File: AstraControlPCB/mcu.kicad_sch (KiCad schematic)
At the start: 9 parts, among them U1 ESP32-S3-WROOM-1U-N8

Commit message: Update wks file
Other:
- company: (none) -> LiveAstra Technologies
- title: MCU -> AstraControl - Root
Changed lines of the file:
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@@
 	(paper "A4")
 	(title_block
-		(title "MCU")
+		(title "AstraControl - Root")
+		(date "2024-08-26")
+		(rev "A")
+		(company "LiveAstra Technologies")
 	)
 	(junction

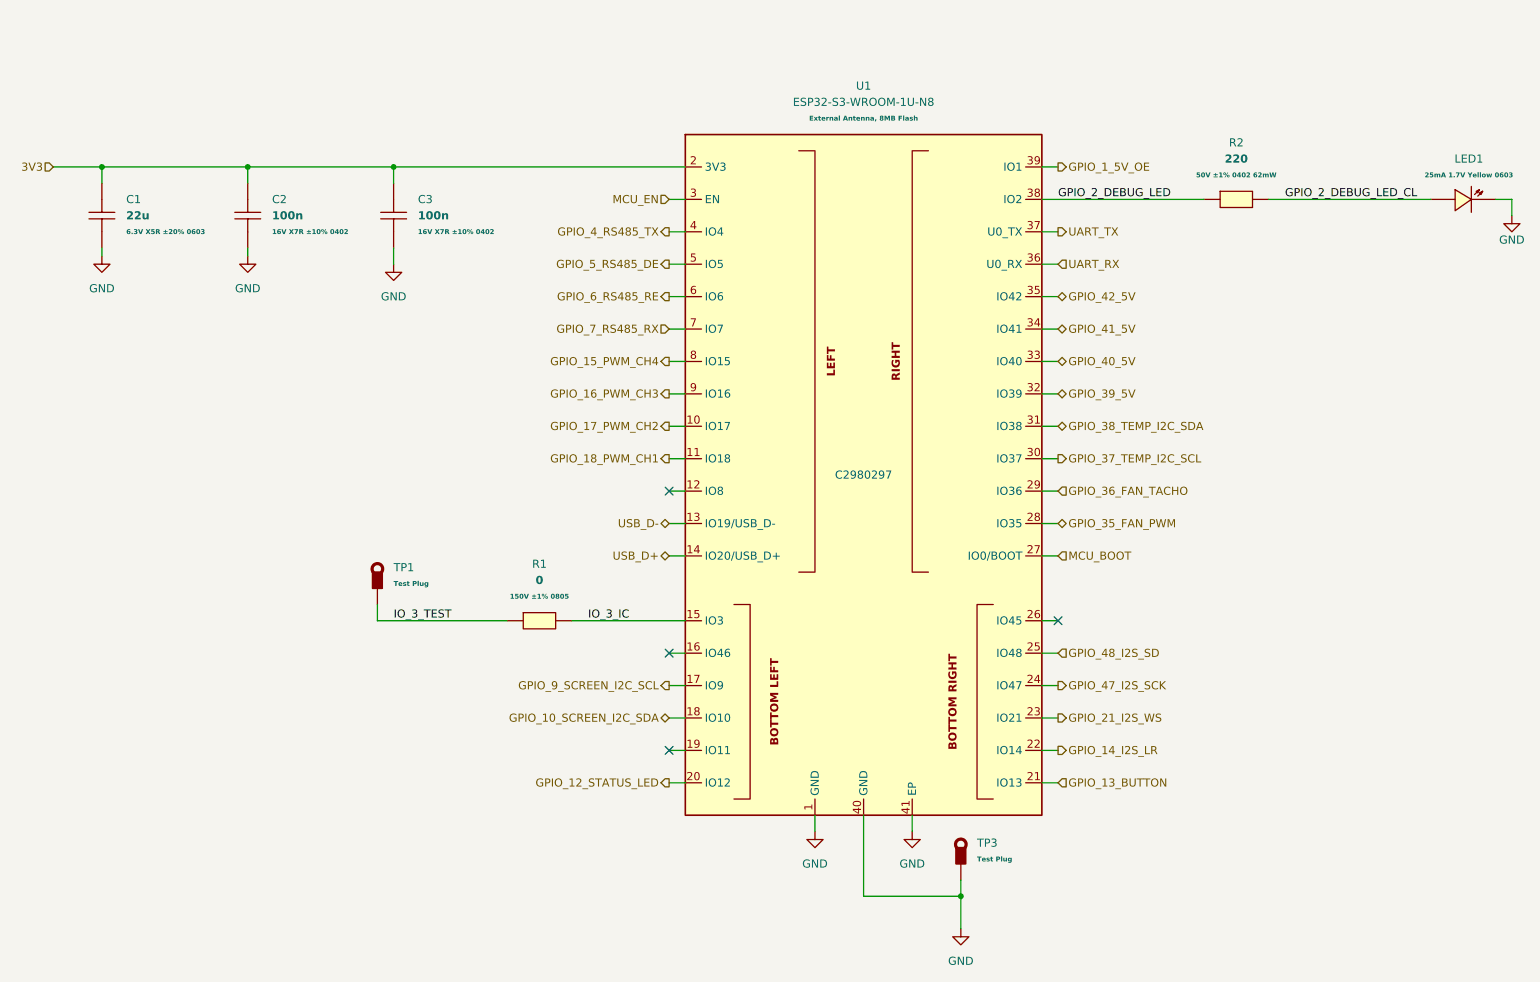
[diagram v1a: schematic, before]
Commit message: Remove plus minus symbol
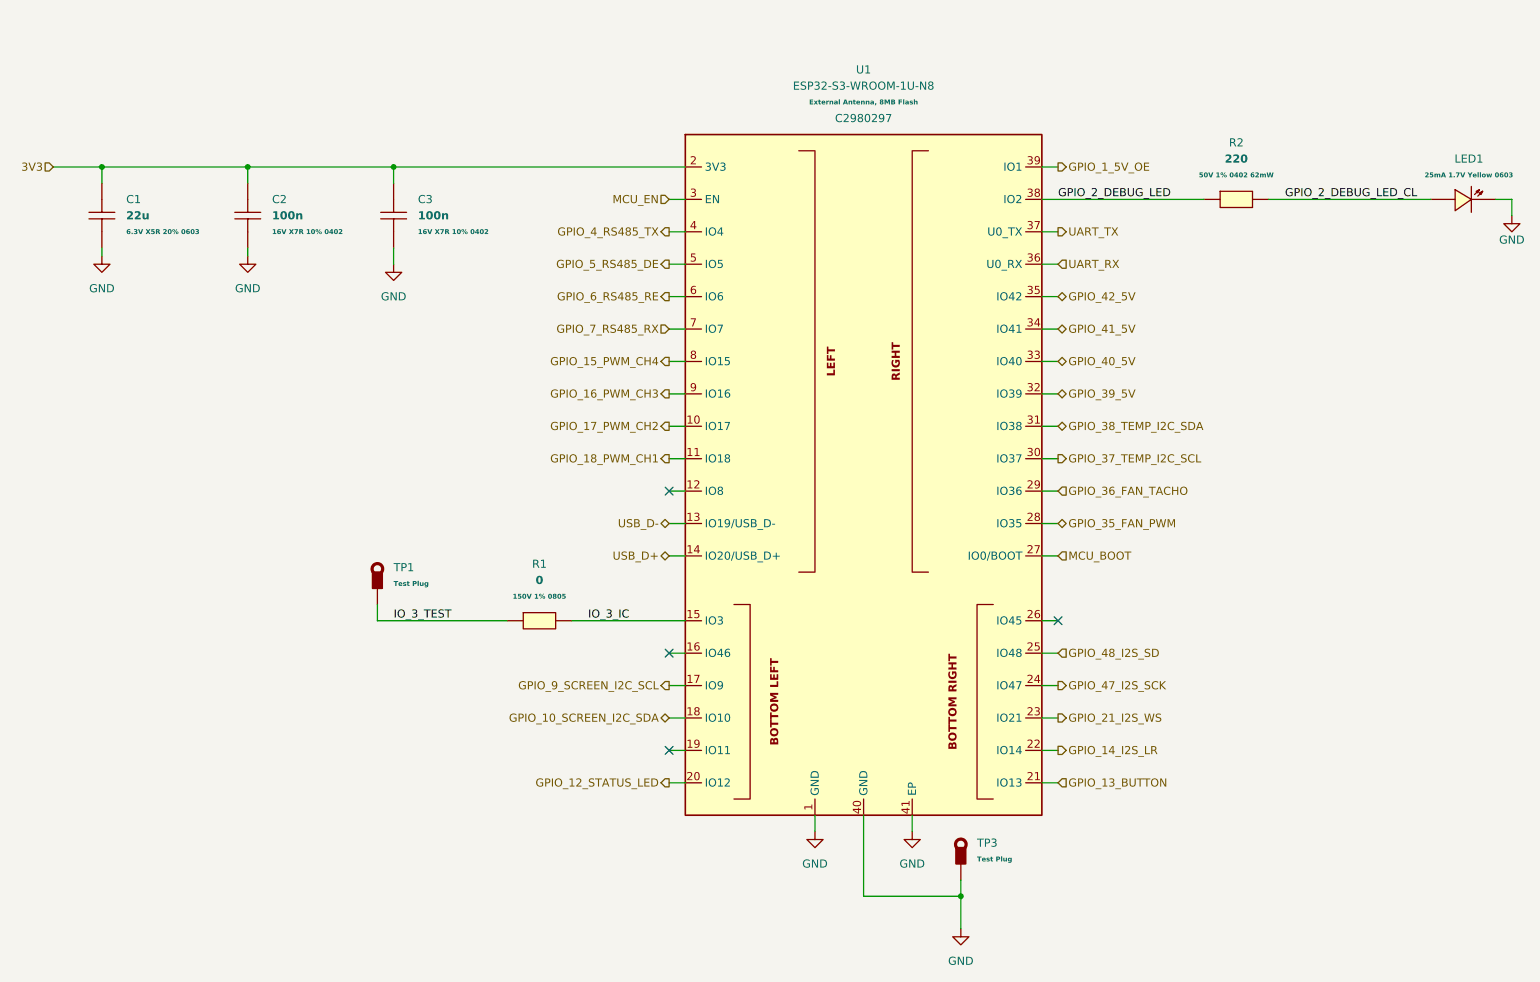
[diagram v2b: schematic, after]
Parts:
- C1: Extra Values 6.3V X5R ±20% 0603 -> 6.3V X5R 20% 0603
- C2, C3: Extra Values 16V X7R ±10% 0402 -> 16V X7R 10% 0402
- R1: Extra Values 150V ±1% 0805 -> 150V 1% 0805
- R2: Extra Values 50V ±1% 0402 62mW -> 50V 1% 0402 62mW
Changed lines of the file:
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@@
 			)
 		)
-		(property "Extra Values" "16V X7R ±10% 0402"
+		(property "Extra Values" "16V X7R 10% 0402"
 			(at 59.69 55.8799 90)
 			(effects
@@
 				)
 				(justify right)
-			)
-		)
-		(property "Extra Value" ""
-			(at 55.88 53.34 0)
-			(effects
-				(font
-					(size 1.27 1.27)
-				)
-				(hide yes)
 			)
 		)
@@
 		(dnp no)
 		(fields_autoplaced yes)
-		(property "Reference" "#PWR05"
+		(property "Reference" "#PWR5"
 			(at 55.88 66.04 0)
 			(effects
@@
 			(project "AstraControl"
 				(path "/9a751838-dce8-4d69-8a02-736625ac74e7/0db21d8e-3390-4d67-877f-0e5d98e37848/3087dd4a-2a8a-4df4-b1d8-8d4a2b3256a2"
-					(reference "#PWR05")
+					(reference "#PWR5")
 					(unit 1)
 				)
@@
 			)
 		)
-		(property "Extra Value" ""
-			(at 246.38 50.8 0)
-			(effects
-				(font
-					(size 1.27 1.27)
-				)
-				(hide yes)
-			)
-		)
 		(pin "1"
 		)
@@
 			)
 		)
-		(property "Extra Values" "6.3V X5R ±20% 0603"
+		(property "Extra Values" "6.3V X5R 20% 0603"
 			(at 36.83 55.8799 90)
 			(effects
@@
 				)
 				(justify right)
-			)
-		)
-		(property "Extra Value" ""
-			(at 33.02 53.34 0)
-			(effects
-				(font
-					(size 1.27 1.27)
-				)
-				(hide yes)
 			)
 		)
@@
 			)
 		)
-		(property "Extra Values" "50V ±1% 0402 62mW"
+		(property "Extra Values" "50V 1% 0402 62mW"
 			(at 210.82 46.99 0)
 			(effects
@@
 					(bold yes)
 				)
-			)
-		)
-		(property "Extra Value" ""
-			(at 210.82 50.8 0)
-			(effects
-				(font
-					(size 1.27 1.27)
-				)
-				(hide yes)
 			)
 		)
@@
 			)
 		)
-		(property "Extra Value" ""
-			(at 167.64 157.48 0)
-			(effects
-				(font
-					(size 1.27 1.27)
-				)
-				(hide yes)
-			)
-		)
 		(pin "1"
 		)
@@
 		(dnp no)
 		(fields_autoplaced yes)
-		(property "Reference" "#PWR04"
+		(property "Reference" "#PWR4"
 			(at 33.02 66.04 0)
 			(effects
@@
 			(project "AstraControl"
 				(path "/9a751838-dce8-4d69-8a02-736625ac74e7/0db21d8e-3390-4d67-877f-0e5d98e37848/3087dd4a-2a8a-4df4-b1d8-8d4a2b3256a2"
-					(reference "#PWR04")
+					(reference "#PWR4")
 					(unit 1)
 				)
@@
 			)
 		)
-		(property "Extra Values" "16V X7R ±10% 0402"
+		(property "Extra Values" "16V X7R 10% 0402"
 			(at 82.55 55.8799 90)
 			(effects
@@
 				)
 				(justify right)
-			)
-		)
-		(property "Extra Value" ""
-			(at 78.74 53.34 0)
-			(effects
-				(font
-					(size 1.27 1.27)
-				)
-				(hide yes)
 			)
 		)
@@
 		(dnp no)
 		(fields_autoplaced yes)
-		(property "Reference" "#PWR06"
+		(property "Reference" "#PWR6"
 			(at 78.74 67.31 0)
 			(effects
@@
 			(project "AstraControl"
 				(path "/9a751838-dce8-4d69-8a02-736625ac74e7/0db21d8e-3390-4d67-877f-0e5d98e37848/3087dd4a-2a8a-4df4-b1d8-8d4a2b3256a2"
-					(reference "#PWR06")
+					(reference "#PWR6")
 					(unit 1)
 				)
@@
 		(dnp no)
 		(fields_autoplaced yes)
-		(property "Reference" "#PWR08"
+		(property "Reference" "#PWR8"
 			(at 160.02 156.21 0)
 			(effects
@@
 			(project "AstraControl"
 				(path "/9a751838-dce8-4d69-8a02-736625ac74e7/0db21d8e-3390-4d67-877f-0e5d98e37848/3087dd4a-2a8a-4df4-b1d8-8d4a2b3256a2"
-					(reference "#PWR08")
+					(reference "#PWR8")
 					(unit 1)
 				)
@@
 		(on_board yes)
 		(dnp no)
-		(property "Reference" "#PWR010"
+		(property "Reference" "#PWR10"
 			(at 254 59.69 0)
 			(effects
@@
 			(project "AstraControl"
 				(path "/9a751838-dce8-4d69-8a02-736625ac74e7/0db21d8e-3390-4d67-877f-0e5d98e37848/3087dd4a-2a8a-4df4-b1d8-8d4a2b3256a2"
-					(reference "#PWR010")
+					(reference "#PWR10")
 					(unit 1)
 				)
@@
 		(dnp no)
 		(fields_autoplaced yes)
-		(property "Reference" "#PWR09"
+		(property "Reference" "#PWR9"
 			(at 167.64 171.45 0)
 			(effects
@@
 			(project "AstraControl"
 				(path "/9a751838-dce8-4d69-8a02-736625ac74e7/0db21d8e-3390-4d67-877f-0e5d98e37848/3087dd4a-2a8a-4df4-b1d8-8d4a2b3256a2"
-					(reference "#PWR09")
+					(reference "#PWR9")
 					(unit 1)
 				)
@@
 		(dnp no)
 		(fields_autoplaced yes)
-		(property "Reference" "#PWR07"
+		(property "Reference" "#PWR7"
 			(at 144.78 156.21 0)
 			(effects
@@
 			(project "AstraControl"
 				(path "/9a751838-dce8-4d69-8a02-736625ac74e7/0db21d8e-3390-4d67-877f-0e5d98e37848/3087dd4a-2a8a-4df4-b1d8-8d4a2b3256a2"
-					(reference "#PWR07")
+					(reference "#PWR7")
 					(unit 1)
 				)
@@
 			)
 		)
-		(property "Extra Values" "150V ±1% 0805"
+		(property "Extra Values" "150V 1% 0805"
 			(at 101.6 113.03 0)
 			(effects
@@
 					(bold yes)
 				)
-			)
-		)
-		(property "Extra Value" ""
-			(at 101.6 116.84 0)
-			(effects
-				(font
-					(size 1.27 1.27)
-				)
-				(hide yes)
 			)
 		)
@@
 		(fields_autoplaced yes)
 		(property "Reference" "U1"
+			(at 152.4 30.48 0)
+			(effects
+				(font
+					(size 1.27 1.27)
+				)
+			)
+		)
+		(property "Value" "ESP32-S3-WROOM-1U-N8"
 			(at 152.4 33.02 0)
-			(effects
-				(font
-					(size 1.27 1.27)
-				)
-			)
-		)
-		(property "Value" "ESP32-S3-WROOM-1U-N8"
-			(at 152.4 35.56 0)
 			(effects
 				(font
@@
 		)
 		(property "Extra Values" "External Antenna, 8MB Flash"
+			(at 152.4 35.56 0)
+			(effects
+				(font
+					(size 0.762 0.762)
+					(bold yes)
+				)
+			)
+		)
+		(property "LCSC Part" "C2980297"
 			(at 152.4 38.1 0)
 			(effects
 				(font
-					(size 0.762 0.762)
-					(bold yes)
-				)
-			)
-		)
-		(property "LCSC Part" "C2980297"
-			(at 152.4 93.98 0)
-			(effects
-				(font
-					(size 1.27 1.27)
-				)
-			)
-		)
-		(property "Extra Value" ""
-			(at 152.4 93.98 0)
-			(effects
-				(font
-					(size 1.27 1.27)
-				)
-				(hide yes)
+					(size 1.27 1.27)
+				)
 			)
 		)
@@
 			)
 		)
-		(property "Extra Value" ""
-			(at 76.2 114.3 0)
-			(effects
-				(font
-					(size 1.27 1.27)
-				)
-				(hide yes)
-			)
-		)

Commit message: workflow
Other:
- note added: "MCU"
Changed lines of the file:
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@@
+		)
+	)
+	(text "MCU"
+		(exclude_from_sim no)
+		(at 19.05 25.4 0)
+		(effects
+			(font
+				(face "ING Me Headline")
+				(size 8 8)
+			)
+			(justify left top)
 		)
 	)
@@
 		(dnp no)
 		(fields_autoplaced yes)
-		(property "Reference" "#PWR5"
+		(property "Reference" "#PWR05"
 			(at 55.88 66.04 0)
 			(effects
@@
 			(project "AstraControl"
 				(path "/9a751838-dce8-4d69-8a02-736625ac74e7/0db21d8e-3390-4d67-877f-0e5d98e37848/3087dd4a-2a8a-4df4-b1d8-8d4a2b3256a2"
-					(reference "#PWR5")
+					(reference "#PWR05")
 					(unit 1)
 				)
@@
 		(dnp no)
 		(fields_autoplaced yes)
-		(property "Reference" "#PWR4"
+		(property "Reference" "#PWR04"
 			(at 33.02 66.04 0)
 			(effects
@@
 			(project "AstraControl"
 				(path "/9a751838-dce8-4d69-8a02-736625ac74e7/0db21d8e-3390-4d67-877f-0e5d98e37848/3087dd4a-2a8a-4df4-b1d8-8d4a2b3256a2"
-					(reference "#PWR4")
+					(reference "#PWR04")
 					(unit 1)
 				)
@@
 		(dnp no)
 		(fields_autoplaced yes)
-		(property "Reference" "#PWR6"
+		(property "Reference" "#PWR06"
 			(at 78.74 67.31 0)
 			(effects
@@
 			(project "AstraControl"
 				(path "/9a751838-dce8-4d69-8a02-736625ac74e7/0db21d8e-3390-4d67-877f-0e5d98e37848/3087dd4a-2a8a-4df4-b1d8-8d4a2b3256a2"
-					(reference "#PWR6")
+					(reference "#PWR06")
 					(unit 1)
 				)
@@
 		(dnp no)
 		(fields_autoplaced yes)
-		(property "Reference" "#PWR8"
+		(property "Reference" "#PWR08"
 			(at 160.02 156.21 0)
 			(effects
@@
 			(project "AstraControl"
 				(path "/9a751838-dce8-4d69-8a02-736625ac74e7/0db21d8e-3390-4d67-877f-0e5d98e37848/3087dd4a-2a8a-4df4-b1d8-8d4a2b3256a2"
-					(reference "#PWR8")
+					(reference "#PWR08")
 					(unit 1)
 				)
@@
 		(on_board yes)
 		(dnp no)
-		(property "Reference" "#PWR10"
+		(property "Reference" "#PWR010"
 			(at 254 59.69 0)
 			(effects
@@
 			(project "AstraControl"
 				(path "/9a751838-dce8-4d69-8a02-736625ac74e7/0db21d8e-3390-4d67-877f-0e5d98e37848/3087dd4a-2a8a-4df4-b1d8-8d4a2b3256a2"
-					(reference "#PWR10")
+					(reference "#PWR010")
 					(unit 1)
 				)
@@
 		(dnp no)
 		(fields_autoplaced yes)
-		(property "Reference" "#PWR9"
+		(property "Reference" "#PWR09"
 			(at 167.64 171.45 0)
 			(effects
@@
 			(project "AstraControl"
 				(path "/9a751838-dce8-4d69-8a02-736625ac74e7/0db21d8e-3390-4d67-877f-0e5d98e37848/3087dd4a-2a8a-4df4-b1d8-8d4a2b3256a2"
-					(reference "#PWR9")
+					(reference "#PWR09")
 					(unit 1)
 				)
@@
 		(dnp no)
 		(fields_autoplaced yes)
-		(property "Reference" "#PWR7"
+		(property "Reference" "#PWR07"
 			(at 144.78 156.21 0)
 			(effects
@@
 			(project "AstraControl"
 				(path "/9a751838-dce8-4d69-8a02-736625ac74e7/0db21d8e-3390-4d67-877f-0e5d98e37848/3087dd4a-2a8a-4df4-b1d8-8d4a2b3256a2"
-					(reference "#PWR7")
+					(reference "#PWR07")
 					(unit 1)
 				)

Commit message: update
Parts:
- renumbered TP3 to TP2
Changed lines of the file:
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@@
 		(dnp no)
 		(fields_autoplaced yes)
-		(property "Reference" "TP3"
+		(property "Reference" "TP2"
 			(at 170.18 151.6676 0)
 			(effects
@@
 			(project "AstraControl"
 				(path "/9a751838-dce8-4d69-8a02-736625ac74e7/0db21d8e-3390-4d67-877f-0e5d98e37848/3087dd4a-2a8a-4df4-b1d8-8d4a2b3256a2"
-					(reference "TP3")
+					(reference "TP2")
 					(unit 1)
 				)

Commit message: Reroute complete
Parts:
- removed C1: 22u, LiveAstra:C_0603_1608Metric, symbol LiveAstra:C_22uF_X5R_0603
- added C19: 47u, LiveAstra:C_0805_2012Metric_Pad1.18x1.45mm_HandSolder, symbol LiveAstra:C_47u_X5R_0805
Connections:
- net 3V3: now also C19.2
- net GND: now also C19.1
- net GPIO_35_FAN_PWM renamed GPIO_35_TEMP_I2C_SCL
- net GPIO_36_FAN_TACHO renamed GPIO_36_TEMP_I2C_SDA
- net GPIO_37_TEMP_I2C_SCL renamed GPIO_37_FAN_PWM
- net GPIO_38_TEMP_I2C_SDA renamed GPIO_38_FAN_TACHO
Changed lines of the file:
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@@
+	(wire
+		(pts
+			(xy 180.34 91.44) (xy 182.88 91.44)
+		)
+		(stroke
+			(width 0)
+			(type default)
+		)
+	)
 	(wire
 		(pts
@@
 	(wire
 		(pts
-			(xy 182.88 91.44) (xy 180.34 91.44)
-		)
-		(stroke
-			(width 0)
-			(type default)
-		)
-	)
-	(wire
-		(pts
 			(xy 33.02 48.26) (xy 33.02 45.72)
 		)
@@
 	(wire
 		(pts
-			(xy 182.88 86.36) (xy 180.34 86.36)
-		)
-		(stroke
-			(width 0)
-			(type default)
-		)
-	)
-	(wire
-		(pts
 			(xy 55.88 48.26) (xy 55.88 45.72)
 		)
@@
 	(wire
 		(pts
+			(xy 180.34 101.6) (xy 182.88 101.6)
+		)
+		(stroke
+			(width 0)
+			(type default)
+		)
+	)
+	(wire
+		(pts
 			(xy 182.88 142.24) (xy 180.34 142.24)
 		)
@@
 	(wire
 		(pts
+			(xy 180.34 86.36) (xy 182.88 86.36)
+		)
+		(stroke
+			(width 0)
+			(type default)
+		)
+	)
+	(wire
+		(pts
 			(xy 121.92 71.12) (xy 124.46 71.12)
 		)
@@
 	(wire
 		(pts
+			(xy 180.34 96.52) (xy 182.88 96.52)
+		)
+		(stroke
+			(width 0)
+			(type default)
+		)
+	)
+	(wire
+		(pts
 			(xy 180.34 71.12) (xy 182.88 71.12)
 		)
@@
 		(pts
 			(xy 180.34 60.96) (xy 182.88 60.96)
-		)
-		(stroke
-			(width 0)
-			(type default)
-		)
-	)
-	(wire
-		(pts
-			(xy 182.88 101.6) (xy 180.34 101.6)
-		)
-		(stroke
-			(width 0)
-			(type default)
-		)
-	)
-	(wire
-		(pts
-			(xy 182.88 96.52) (xy 180.34 96.52)
 		)
 		(stroke
@@
 		)
 	)
-	(hierarchical_label "GPIO_38_TEMP_I2C_SDA"
+	(hierarchical_label "GPIO_36_TEMP_I2C_SDA"
 		(shape bidirectional)
-		(at 182.88 86.36 0)
+		(at 182.88 96.52 0)
 		(fields_autoplaced yes)
 		(effects
@@
 		)
 	)
-	(hierarchical_label "GPIO_37_TEMP_I2C_SCL"
+	(hierarchical_label "GPIO_35_TEMP_I2C_SCL"
 		(shape output)
-		(at 182.88 91.44 0)
+		(at 182.88 101.6 0)
 		(fields_autoplaced yes)
 		(effects
@@
 		)
 	)
-	(hierarchical_label "GPIO_35_FAN_PWM"
+	(hierarchical_label "GPIO_37_FAN_PWM"
 		(shape bidirectional)
-		(at 182.88 101.6 0)
+		(at 182.88 91.44 0)
 		(fields_autoplaced yes)
 		(effects
@@
 		)
 	)
-	(hierarchical_label "GPIO_36_FAN_TACHO"
+	(hierarchical_label "GPIO_38_FAN_TACHO"
 		(shape input)
-		(at 182.88 96.52 0)
+		(at 182.88 86.36 0)
 		(fields_autoplaced yes)
 		(effects
@@
 				(path "/9a751838-dce8-4d69-8a02-736625ac74e7/0db21d8e-3390-4d67-877f-0e5d98e37848/3087dd4a-2a8a-4df4-b1d8-8d4a2b3256a2"
 					(reference "LED1")
-					(unit 1)
-				)
-			)
-		)
-	)
-	(symbol
-		(lib_id "LiveAstra:C_22uF_X5R_0603")
-		(at 33.02 53.34 90)
-		(unit 1)
-		(exclude_from_sim no)
-		(in_bom yes)
-		(on_board yes)
-		(dnp no)
-		(fields_autoplaced yes)
-		(property "Reference" "C1"
-			(at 36.83 50.7999 90)
-			(effects
-				(font
-					(size 1.27 1.27)
-				)
-				(justify right)
-			)
-		)
-		(property "Value" "22u"
-			(at 36.83 53.34 90)
-			(effects
-				(font
-					(size 1.27 1.27)
-					(bold yes)
-				)
-				(justify right)
-			)
-		)
-		(property "Footprint" "LiveAstra:C_0603_1608Metric"
-			(at 41.91 53.34 0)
-			(effects
-				(font
-					(size 1.27 1.27)
-				)
-				(hide yes)
-			)
-		)
-		(property "Datasheet" "https://lcsc.com/product-detail/Multilayer-Ceramic-Capacitors-MLCC-SMD-SMT_SAMSUNG_CL10A226MQ8NRNC_22uF-226-20-6-3V_C59461.html"
-			(at 45.72 53.34 0)
-			(effects
-				(font
-					(size 1.27 1.27)
-				)
-				(hide yes)
-			)
-		)
-		(property "Description" "Multilayer Ceramic Capacitor"
-			(at 38.1 53.34 0)
-			(effects
-				(font
-					(size 1.27 1.27)
-				)
-				(hide yes)
-			)
-		)
-		(property "LCSC Part" "C59461"
-			(at 49.53 53.34 0)
-			(effects
-				(font
-					(size 1.27 1.27)
-				)
-				(hide yes)
-			)
-		)
-		(property "Extra Values" "6.3V X5R 20% 0603"
-			(at 36.83 55.8799 90)
-			(effects
-				(font
-					(size 0.762 0.762)
-					(bold yes)
-				)
-				(justify right)
-			)
-		)
-		(pin "2"
-		)
-		(pin "1"
-		)
-		(instances
-			(project "AstraControl"
-				(path "/9a751838-dce8-4d69-8a02-736625ac74e7/0db21d8e-3390-4d67-877f-0e5d98e37848/3087dd4a-2a8a-4df4-b1d8-8d4a2b3256a2"
-					(reference "C1")
 					(unit 1)
 				)
@@
 					(unit 1)
 				)
+			)
+		)
+	)
+	(symbol
+		(lib_id "LiveAstra:C_47u_X5R_0805")
+		(at 33.02 53.34 90)
+		(unit 1)
+		(exclude_from_sim no)
+		(in_bom yes)
+		(on_board yes)
+		(dnp no)
+		(fields_autoplaced yes)
+		(property "Reference" "C19"
+			(at 36.83 50.7999 90)
+			(effects
+				(font
+					(size 1.27 1.27)
+				)
+				(justify right)
+			)
+		)
+		(property "Value" "47u"
+			(at 36.83 53.34 90)
+			(effects
+				(font
+					(size 1.27 1.27)
+					(bold yes)
+				)
+				(justify right)
+			)
+		)
+		(property "Footprint" "LiveAstra:C_0805_2012Metric_Pad1.18x1.45mm_HandSolder"
+			(at 41.91 53.34 0)
+			(effects
+				(font
+					(size 1.27 1.27)
+				)
+				(hide yes)
+			)
+		)
+		(property "Datasheet" "https://lcsc.com/product-detail/Multilayer-Ceramic-Capacitors-MLCC-SMD-SMT_SAMSUNG_CL21A476MQYNNNE_47uF-476-20-6-3V_C16780.html"
+			(at 45.72 53.34 0)
+			(effects
+				(font
+					(size 1.27 1.27)
+				)
+				(hide yes)
+			)
+		)
+		(property "Description" "Multilayer Ceramic Capacitor"
+			(at 38.1 53.34 0)
+			(effects
+				(font
+					(size 1.27 1.27)
+				)
+				(hide yes)
+			)
+		)
+		(property "LCSC Part" "C16780"
+			(at 49.53 53.34 0)
+			(effects
+				(font
+					(size 1.27 1.27)
+				)
+				(hide yes)
+			)
+		)
+		(property "Extra Values" "6.3V X5R 20% 0805"
+			(at 36.83 55.8799 90)
+			(effects
+				(font
+					(size 0.762 0.762)
+					(bold yes)
+				)
+				(justify right)
+			)
+		)
+		(pin "1"
+		)
+		(pin "2"
+		)
+		(instances
+			(project ""
+				(path "/9a751838-dce8-4d69-8a02-736625ac74e7/0db21d8e-3390-4d67-877f-0e5d98e37848/3087dd4a-2a8a-4df4-b1d8-8d4a2b3256a2"
+					(reference "C19")
+					(unit 1)
+				)

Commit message: Updates
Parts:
- renumbered C19 to C1
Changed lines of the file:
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@@
 			)
 		)
-		(property "Datasheet" ""
+		(property "Datasheet" "https://www.lcsc.com/product-detail/Thimble-Copper-Rod-Test-Ring_ronghe-RH-5000_C5277086.html"
 			(at 167.64 152.4 90)
 			(effects
@@
 		(dnp no)
 		(fields_autoplaced yes)
-		(property "Reference" "C19"
+		(property "Reference" "C1"
 			(at 36.83 50.7999 90)
 			(effects
@@
 			(project ""
 				(path "/9a751838-dce8-4d69-8a02-736625ac74e7/0db21d8e-3390-4d67-877f-0e5d98e37848/3087dd4a-2a8a-4df4-b1d8-8d4a2b3256a2"
-					(reference "C19")
+					(reference "C1")
 					(unit 1)
 				)
@@
 			)
 		)
-		(property "Datasheet" ""
+		(property "Datasheet" "https://www.lcsc.com/product-detail/Thimble-Copper-Rod-Test-Ring_ronghe-RH-5000_C5277086.html"
 			(at 76.2 109.22 90)
 			(effects
